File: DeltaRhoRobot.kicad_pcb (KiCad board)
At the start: 4 copper layers, 75 x 100 mm, 121 parts, among them J1 Conn_01x02_Socket, J10 Conn_01x02, J11 Conn_01x08, J12 USB_C_Receptacle_USB2.0, J13 Conn_02x09_Top_Bottom, J14 Conn_01x09, J15 Conn_02x09_Top_Bottom, J2 USB_C_Receptacle_USB2.0, J3 USB_C_Receptacle_USB2.0, J4 B4B-ZRLFSN, J5 B4B-ZRLFSN, J6 Conn_01x09, J7 Conn_02x20_Counter_Clockwise, P1 B6B-ZRLFSN, P2 B6B-ZRLFSN, P3 B6B-ZRLFSN, P4 S6B-ZRLFSN, P5 B6B-ZRLFSN, P6 B6B-ZRLFSN, Q1 MBT3904DW1, Q2 BSS138, Q3 STB55NF06T4, Q5 BSS138, SW1 CAS-120A1, SW4 SW_Push, U1 AP63205WU-7, U10 ICM-20948, U11 FT231XS, U12 ESP32-CAM, U13 MIC5365-3.3YC5, U2 AMS1117-3.3, U3 DRV8835DSSR, U4 RP2040, U5 DRV8835DSSR, U6 DRV8835DSSR, U7 W25X40CLSS, U8 ESP32-S3-WROOM-1-N8R2, Y1 ABM8G-12.000MHZ-4Y-T3

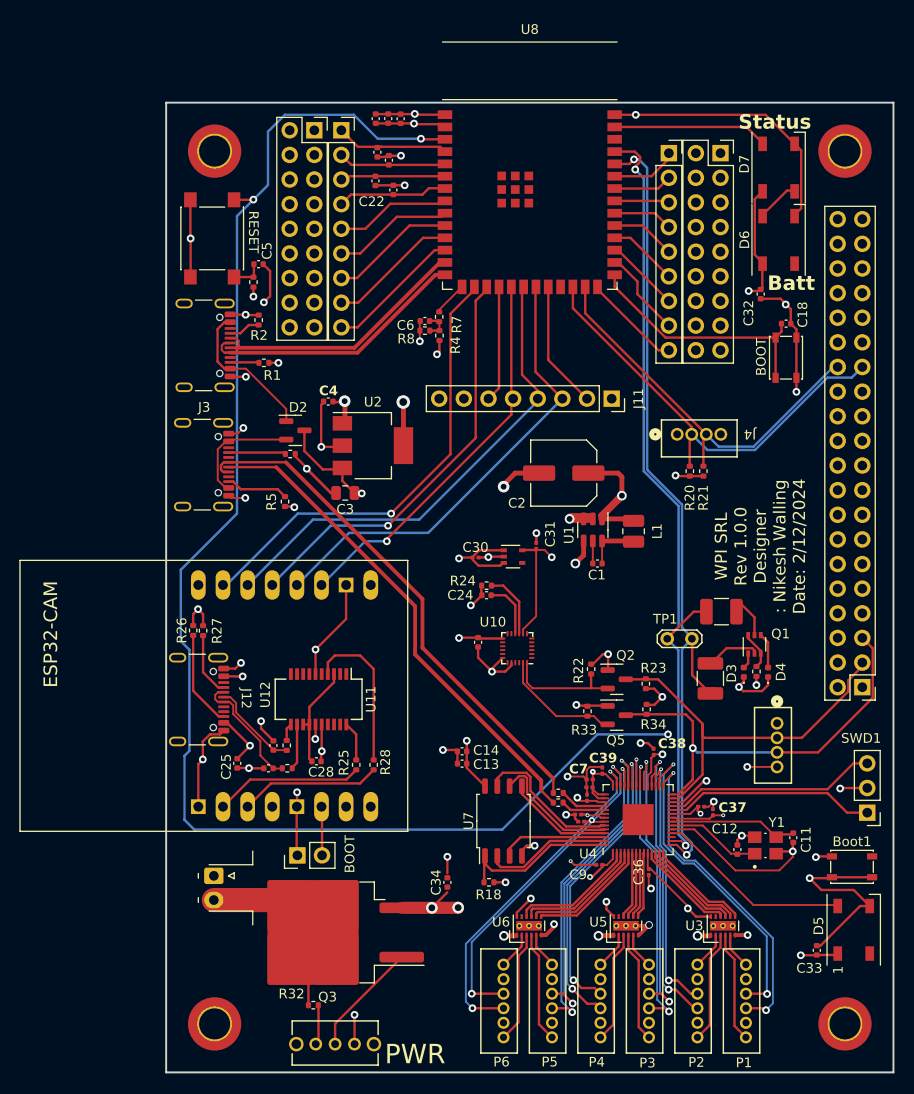
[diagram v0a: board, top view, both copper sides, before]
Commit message: Removed 201-sized parts
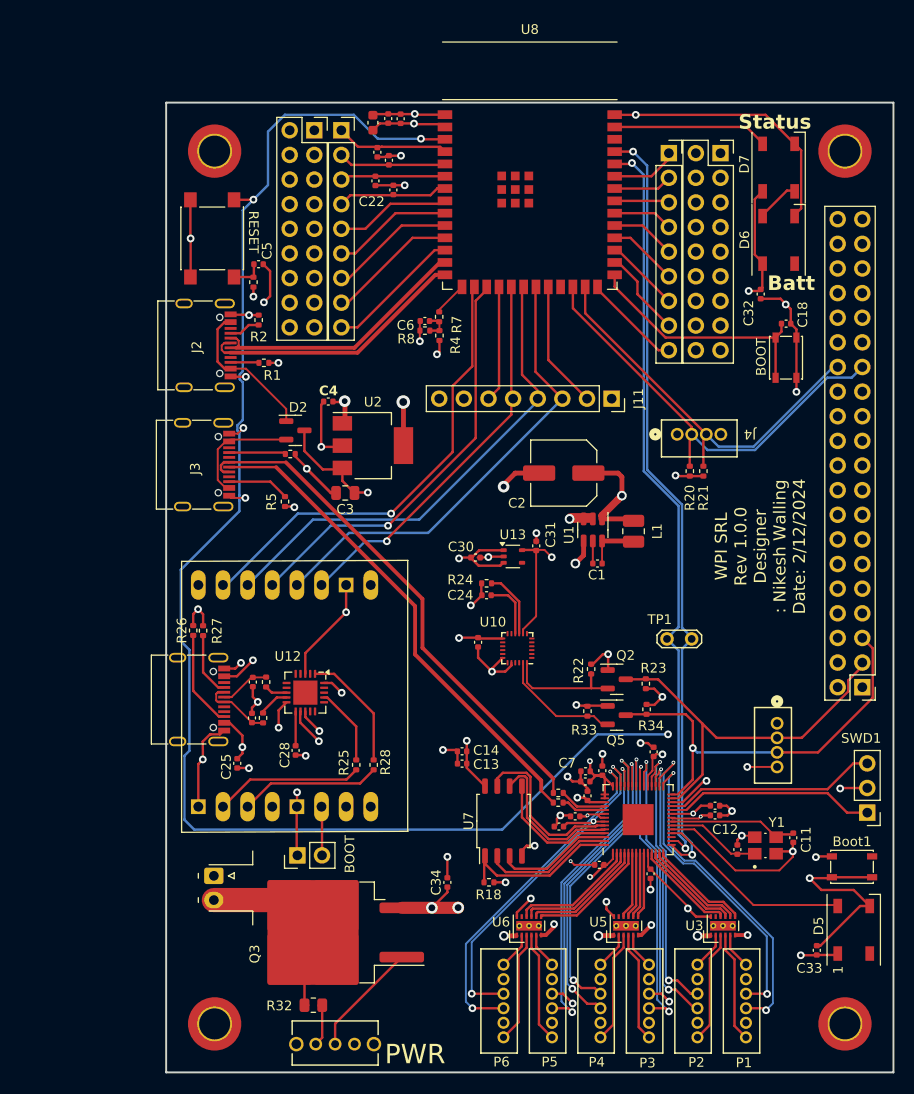
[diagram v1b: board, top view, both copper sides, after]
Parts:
- removed D3, D4: LED, LED_SMD:LED_0402_1005Metric
- removed Q1: MBT3904DW1, Package_TO_SOT_SMD:SOT-363_SC-70-6
- removed R10: 220, Resistor_SMD:R_0402_1005Metric
- removed R12, R13: 1k, Resistor_SMD:R_1210_3225Metric_Pad1.30x2.65mm_HandSolder
- removed U11: FT231XS, Package_SO:SSOP-20_3.9x8.7mm_P0.635mm
- added U9: FT231XQ, Package_DFN_QFN:QFN-20-1EP_4x4mm_P0.5mm_EP2.5x2.5mm, F.Cu at (164.4, 110.8)
- C10, C30, C31, C35, C36, C37, C38, C39, C40, C41, C42, C7, C9: footprint Capacitor_SMD:C_0201_0603Metric -> Capacitor_SMD:C_0402_1005Metric
- C11, C12: value 15p -> 15pF
- C14: value 100n -> 100nF
- C15, C18, C19, C20, C21, C22, C28: value 0.1uF -> 100nF
- C16: value 1uf -> 1uF
- C17: footprint Capacitor_SMD:C_0402_1005Metric -> Capacitor_SMD:C_0603_1608Metric
- C23, C24: value 0.1uf -> 100nF
- C34: value .1uf -> 100nF
- C5: value .1uF -> 100nf
- J12, J2, J3: footprint Connector_USB:USB_C_Receptacle_GCT_USB4105-xx-A_16P_TopMnt_Horizontal -> Connector_USB:USB_C_Receptacle_G-Switch_GT-USB-7010ASV
- R32: value 68k -> 66.5k; footprint Resistor_SMD:R_0402_1005Metric -> Resistor_SMD:R_0805_2012Metric
- R4: value 10k -> 22k
- Y1: value ABM8G-12.000MHZ-4Y-T3 -> FL1200060
- moved C26 6.87 mm to (158.9, 109.8), turned to -90 degrees
- moved R30 6.87 mm to (160.3, 109.7), turned to 90 degrees
- moved R29 5.76 mm to (160.0, 113.5), turned to 90 degrees
- moved C27 5.47 mm to (158.8, 113.5), turned to 90 degrees
- moved TP1 2.57 mm to (201.7, 105.3), turned to 0 degrees
- moved C28 2.42 mm to (163.3, 116.8), turned to -90 degrees
- moved C42 2.36 mm to (190.5, 124.7)
- moved C10 1.41 mm to (206.6, 122.5)
- moved C7 0.95 mm to (193.2, 119.0)
- moved C41 0.74 mm to (193.2, 120.0)
- moved C17 0.51 mm to (171.3, 52.1)
- moved C37 0.39 mm to (206.6, 123.5), turned to 180 degrees
- moved C40 0.36 mm to (192.2, 123.6)
- moved C36 0.25 mm to (199.9, 129.5)
- moved R24 0.24 mm to (183.0, 99.6)
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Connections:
- C28 pad 1: /ESP32-S3-WROOM-1/ESP32CAM/3.3V_Out -> Net-(U9-~{RESET})
- R29 pad 2: /ESP32-S3-WROOM-1/ESP32CAM/3.3V_Out -> Net-(U9-USBDM)
- R30 pad 1: /ESP32-S3-WROOM-1/ESP32CAM/3.3V_Out -> Net-(U9-USBDP)
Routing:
- net Earth: track 233.4 -> 222.0 mm
- net Pico_SDA1: track 86.9 -> 77.1 mm
- net /ESP32-S3-WROOM-1/ESP32CAM/V_USB: track 23.2 -> 29.1 mm
- net /ESP32-S3-WROOM-1/ESP32CAM/ESPCAM_USB_D-: track 12.7 -> 7.32 mm
- net Net-(Q1A-B1): track 4.76 -> 0.00 mm
- net /ESP32-S3-WROOM-1/ESP32CAM/ESPCAM_USB_D+: track 9.30 -> 5.18 mm
- net Net-(Q1A-C1): track 3.96 -> 0.00 mm
- net Net-(U9-TXD): track 4.08 -> 8.00 mm
- net Net-(Q1B-B2): track 3.92 -> 0.00 mm
- net Net-(D4-A): track 3.65 -> 0.00 mm
- net Net-(U9-RXD): track 16.2 -> 12.5 mm
- net Pico_SCL1: track 84.0 -> 80.4 mm
- net Net-(U9-~{RESET}): track 0.00 -> 3.56 mm
- net Net-(U9-USBDM): track 0.00 -> 3.19 mm
- net /ESP32-S3-WROOM-1/ESP32CAM/3.3V_Out: track 17.3 -> 14.5 mm, vias 0 -> 2
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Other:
- board text removed: "If UART R=1k"

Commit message: Replacing ICM-20948
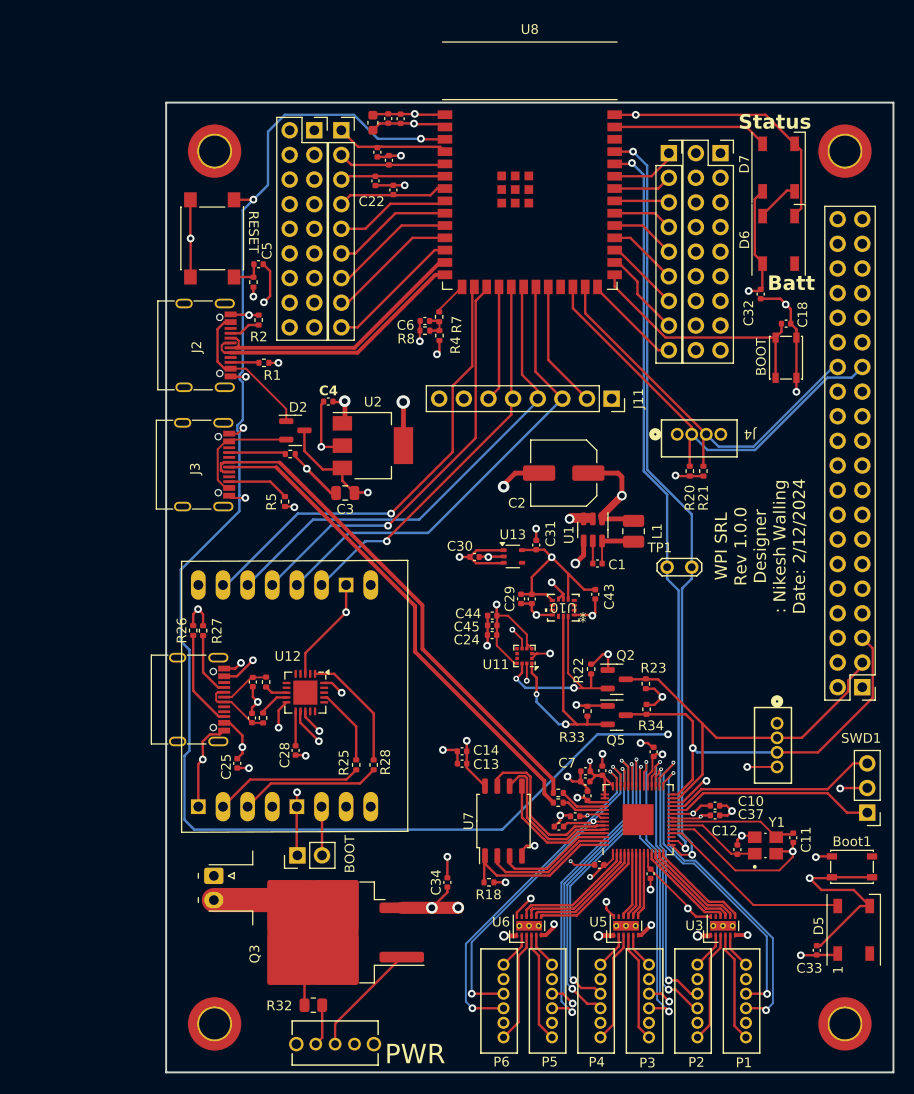
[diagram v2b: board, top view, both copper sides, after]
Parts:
- removed R24: 47, Resistor_SMD:R_0402_1005Metric
- added C29: 2.2uF, Capacitor_SMD:C_0402_1005Metric, F.Cu at (186.6, 101.2)
- added C43: 10nF, Capacitor_SMD:C_0402_1005Metric, F.Cu at (194.2, 100.7)
- added C44: 100nF, Capacitor_SMD:C_0402_1005Metric, F.Cu at (183.6, 102.9)
- added C45: 1uF, Capacitor_SMD:C_0402_1005Metric, F.Cu at (183.6, 103.9)
- added U11: LIS3MDL, Package_LGA:LGA-12_2x2mm_P0.5mm, F.Cu at (186.9, 107.1)
- U10: value ICM-20948 -> ICM-42688-P; footprint Sensor_Motion:InvenSense_QFN-24_3x3mm_P0.4mm -> ICM-42688:LGA14_2P5X3X0P91_TDK
- moved TP1 7.40 mm to (201.7, 97.9)
- moved C23 7.12 mm to (187.7, 101.2)
- moved U10 6.33 mm to (191.0, 102.1)
- moved C24 4.14 mm to (183.6, 104.9)
- moved C30 0.12 mm to (181.8, 96.8)
- moved C31 0.09 mm to (188.2, 95.6)
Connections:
- C23 pad 1: +3.3V -> +1V8
- C24 pad 1: Net-(U10-REGOUT) -> +3.3V
- U10 pad 1: unconnected-(U10-NC-Pad1) -> Earth
- U10 pad 10: Net-(U10-REGOUT) -> unconnected-(U10-RESV-Pad10)
- U10 pad 11: unconnected-(U10-FSYNC-Pad11) -> Earth
- U10 pad 12: unconnected-(U10-INT1-Pad12) -> +1V8
- U10 pad 13: +3.3V -> /Pico/IMU/SCL
- U10 pad 14: unconnected-(U10-NC-Pad14) -> /Pico/IMU/SDA
- U10 pad 5: unconnected-(U10-NC-Pad5) -> +1V8
- U10 pad 6: unconnected-(U10-NC-Pad6) -> Earth
- U10 pad 7: unconnected-(U10-AUX_CL-Pad7) -> Earth
- U10 pad 9: Net-(U10-SDO/AD0) -> unconnected-(U10-INT2/FSYNC/CLKIN-Pad9)
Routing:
- net +1V8: track 42.2 -> 59.7 mm, vias 3 -> 4
- net /Pico/IMU/SCL: track 11.9 -> 25.1 mm, vias 0 -> 2
- net /Pico/IMU/SDA: track 11.6 -> 20.6 mm, vias 0 -> 2
- net +3.3V: track 84.1 -> 92.5 mm
- net Earth: track 222.0 -> 229.9 mm, vias 50 -> 54
- net Net-(U10-SDO/AD0): track 6.89 -> 0.00 mm
- net Net-(U10-REGOUT): track 6.16 -> 0.00 mm
- net VS: track 10.7 -> 9.58 mm
- net /ESP32-S3-WROOM-1/GPIO_18: track 13.5 -> 12.8 mm
- net Pico_SDA1: track 77.1 -> 76.5 mm
- net Net-(SW1-A): track 4.03 -> 3.49 mm

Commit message: For production
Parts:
- C13: value 2.2u -> 2.2uF
- C17: value 22uf -> 22uF
- C35, C41: value 1uf -> 1uF
- C5: value 100nf -> 100nF
- R15, R16, R29, R30: value 27 -> 33
- R18: value 1k -> 1K
- R20, R21: value 5k -> 5K
- R32: value 66.5k -> 68k
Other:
- outline, holes or cut-outs redrawn
- board text added: "WPI SRL Rev 1.0.0 Designer: Nikesh Walling Date: 5/20/2024"
- board text added: "X"
- board text added: "Y"
- board text added: "Z"
- board text removed: "WPI SRL Rev 1.0.0 Designer : Nikesh Walling Date: 2/12/2024"

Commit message: JLCniceness
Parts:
- J4, J5: value B4B-ZRLFSN -> JST-XH; footprint JST-ZR-4Pin:CONN_B4B-ZRLFSN_JST -> Connector_JST:JST_XH_B4B-XH-AM_1x04_P2.50mm_Vertical
- moved R20 9.01 mm to (212.6, 85.3), turned to 180 degrees
- moved R21 8.82 mm to (212.6, 82.9), turned to 0 degrees
- moved J4 6.56 mm to (204.7, 90.5), turned to 90 degrees
- moved J5 3.93 mm to (210.3, 116.8)
- moved R2 0.96 mm to (160.3, 73.0)
- moved C15 0.54 mm to (174.1, 52.2)
- moved C16 0.54 mm to (172.8, 52.2)
- moved C17 0.54 mm to (171.2, 52.6)
- moved C18 0.52 mm to (213.4, 72.8)
- moved SW4 0.52 mm to (213.4, 76.3)
- moved R30 0.32 mm to (160.0, 109.8)
- moved C26 0.09 mm to (158.8, 109.8)
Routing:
- net PICO_SCL: track 43.2 -> 37.1 mm
- net +5V: track 136.8 -> 132.6 mm
- net /Pico/M5_Enc_B: track 32.4 -> 35.4 mm
- net Earth: track 229.8 -> 232.5 mm, vias 54 -> 50
- net /V_USB_2: track 11.2 -> 13.9 mm, vias 0 -> 2
- net /ESP32-S3-WROOM-1/SCL: track 40.4 -> 38.4 mm
- net +3.3V: track 92.5 -> 90.5 mm, vias 17 -> 18
- net /Pico/M4_Enc_A: track 31.9 -> 33.7 mm
- net /Pico/M5_Enc_A: track 33.9 -> 35.5 mm
- net /Pico/M3_Enc_A: track 30.7 -> 32.2 mm
- net /V_USB_1: track 15.3 -> 16.4 mm, vias 0 -> 2
- net /Pico/M4_Enc_B: track 32.3 -> 33.4 mm
- net PICO_SDA: track 40.1 -> 39.1 mm
- net /Pico/M6_Enc_A: track 35.6 -> 34.7 mm
- net /Pico/M3_Enc_B: track 30.7 -> 31.5 mm
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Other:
- board text added: "WPI SRL Rev 1.0.1 Designer: Nikesh Walling Date: 5/20/2024"
- board text removed: "WPI SRL Rev 1.0.0 Designer: Nikesh Walling Date: 5/20/2024"

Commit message: JLC fixes
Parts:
- J4, J5: footprint Connector_JST:JST_XH_B4B-XH-AM_1x04_P2.50mm_Vertical -> Connector_JST:JST_XH_B4B-XH-A_1x04_P2.50mm_Vertical
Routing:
- net /Pico/M5_Enc_B: track 35.4 -> 39.2 mm
- net /ESP_PU: track 166.1 -> 168.8 mm
- net +1V8: track 59.6 -> 62.2 mm, vias 4 -> 5
- net /Pico/M6_Enc_A: track 34.7 -> 37.2 mm
- net /Pico/M3_Enc_B: track 31.5 -> 33.2 mm
- net /Pico/M4_Enc_B: track 33.4 -> 35.0 mm
- net +3.3V: track 90.5 -> 89.0 mm
- net /Pico/M2_Enc_A: track 27.7 -> 29.0 mm
- net /ESP32-S3-WROOM-1/ESP_MOSI: track 40.2 -> 41.2 mm
- net /ESP32-S3-WROOM-1/Handshake: track 46.4 -> 47.3 mm
- net /ESP32-S3-WROOM-1/ESP_CS1: track 43.0 -> 43.9 mm
- net /Pico/M5_Enc_A: track 35.5 -> 34.5 mm
- net /Pico/M6_Enc_B: track 35.9 -> 36.8 mm
- net /V_USB_2: track 13.9 -> 14.6 mm
- net Earth: track 232.5 -> 233.2 mm
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
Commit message: Rev 2 PCB
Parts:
- removed C34: 100nF, Capacitor_SMD:C_0402_1005Metric
- removed D2: PMEG2005CT, Package_TO_SOT_SMD:SOT-23
- removed Q3: STB55NF06T4, Package_TO_SOT_SMD:TO-263-2
- removed R32: 68k, Resistor_SMD:R_0805_2012Metric
- removed U1: AP63205WU-7, Package_TO_SOT_SMD:TSOT-23-6
- added C46: 100nF, Capacitor_SMD:C_0402_1005Metric, F.Cu at (190.3, 93.9)
- added C47: 22uF, Capacitor_SMD:C_0805_2012Metric, F.Cu at (191.1, 85.6)
- added C48: 10uF, Capacitor_SMD:C_0402_1005Metric, F.Cu at (189.2, 93.9)
- added C49: 100nF, Capacitor_SMD:C_0402_1005Metric, F.Cu at (189.2, 86.7)
- added C50: 22uF, Capacitor_SMD:C_0805_2012Metric, F.Cu at (164.3, 133.8)
- added C51: 22uF, Capacitor_SMD:C_0805_2012Metric, F.Cu at (197.6, 85.6)
- added C52: 22uF, Capacitor_SMD:C_0805_2012Metric, F.Cu at (193.3, 85.6)
- added C53: 22uF, Capacitor_SMD:C_0805_2012Metric, F.Cu at (195.5, 85.6)
- added C54: 22uF, Capacitor_SMD:C_0805_2012Metric, F.Cu at (161.0, 133.8)
- added D1: PMEG2005CT, Package_TO_SOT_SMD:SOT-23, F.Cu at (163.3, 83.8)
- added MOSFET1: AONR21321, AONR:DFN8_3x3_EP_AOS, F.Cu at (168.4, 137.5)
- added R10: 30K, Resistor_SMD:R_0402_1005Metric, F.Cu at (197.4, 92.0)
- added R11: R_US, Resistor_SMD:R_0402_1005Metric, F.Cu at (209.5, 124.2)
- added R12: 27, Resistor_SMD:R_0402_1005Metric, F.Cu at (167.4, 142.3)
- added R13: 100K, Resistor_SMD:R_0402_1005Metric, F.Cu at (193.9, 96.1)
- added R17: DNF, Resistor_SMD:R_0603_1608Metric_Pad0.98x0.95mm_HandSolder, F.Cu at (179.7, 121.5)
- added R19: 33.2K, Resistor_SMD:R_0402_1005Metric, F.Cu at (193.9, 97.3)
- added R3: 220K, Resistor_SMD:R_0402_1005Metric, F.Cu at (196.9, 90.2)
- added R9: 1K, Resistor_SMD:R_0402_1005Metric, F.Cu at (163.0, 142.3)
- added TP2: TestPoint, TestPoint:TestPoint_Pad_D1.5mm, F.Cu at (179.5, 127.8)
- added U14: W25Q16JVS, Package_SO:SOIC-8_5.23x5.23mm_P1.27mm, F.Cu at (184.8, 124.0)
- C1: value 100nF -> 10uF
- C2: value 22uF -> 33pF; footprint Capacitor_SMD:C_Elec_6.3x5.8 -> Capacitor_SMD:C_0402_1005Metric
- C3: footprint Capacitor_SMD:C_0805_2012Metric -> Capacitor_SMD:C_0402_1005Metric
- L1: value 4.7uH -> 2.2uH
- P4: value S6B-ZRLFSN -> B6B-ZRLFSN
- R16: value 33 -> 27
- U7: value W25X40CLSS -> TPS566242DRLR; footprint Package_SO:SOIC-8_5.275x5.275mm_P1.27mm -> Package_TO_SOT_SMD:SOT-23-6
- U8: footprint Espressif:ESP32-S3-WROOM-1 -> PCM_Espressif:ESP32-S3-WROOM-1
- Y1: value FL1200060 -> ABM8-272-T3; footprint ABM8G:XTAL_ABM8G-12.000MHZ-4Y-T3 -> Oscillator:Oscillator_SMD_Abracon_ASE-4Pin_3.2x2.5mm
- moved U7 33.0 mm to (194.0, 92.4), turned to 0 degrees
- moved R20 22.8 mm to (192.9, 73.9), turned to 90 degrees
- moved R21 19.3 mm to (195.4, 74.1), turned to -90 degrees
- moved L1 9.64 mm to (189.3, 90.5)
- moved C2 7.38 mm to (198.1, 90.2), turned to -90 degrees
- moved C1 7.25 mm to (188.2, 93.9), turned to -90 degrees
- moved J4 4.88 mm to (209.6, 90.4)
- moved C4 3.97 mm to (170.3, 79.1), turned to 180 degrees
- moved C31 3.32 mm to (188.7, 98.9), turned to -90 degrees
- moved R26 2.97 mm to (155.7, 103.9), turned to 0 degrees
- moved J1 2.00 mm to (154.3, 131.7)
- moved R27 1.95 mm to (155.7, 104.9), turned to 0 degrees
- moved C30 1.92 mm to (181.3, 98.7), turned to 90 degrees
- moved U13 1.81 mm to (184.6, 98.2)
- moved C42 1.24 mm to (189.6, 123.8), turned to 90 degrees
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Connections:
- C1 pad 1: Net-(U1-SW) -> VCC
- C1 pad 2: Net-(U1-BST) -> Earth
- C11 pad 1: /Pico/XOUT -> Net-(C11-Pad1)
- C2 pad 2: Earth -> Net-(U7-FB)
- C3 pad 1: VCC -> +5V
- J1 pad 2: VS -> VIN
- J11 pad 8: VCC -> +5V
- L1 pad 1: Net-(U1-BST) -> Net-(U7-SW)
- U2 pad 3: VCC -> +5V
- U7 pad 1: /Pico/QSPI_SDSS -> Earth
- U7 pad 2: /Pico/QSPI_SD1 -> Net-(U7-SW)
- U7 pad 3: /Pico/QSPI_SD2 -> VCC
- U7 pad 5: /Pico/QSPI_SD0 -> Net-(U7-EN)
- U7 pad 6: /Pico/QSPI_SCK -> Net-(U7-FB)
- Y1 pad 3: /Pico/XOUT -> Net-(C11-Pad1)
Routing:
- net +5V: track 132.6 -> 199.7 mm, vias 3 -> 5
- net VIN: track 0.00 -> 26.6 mm
- net /ESP_PU: track 168.8 -> 154.5 mm
- net VS: track 9.58 -> 0.00 mm
- net Earth: track 233.2 -> 242.7 mm, vias 50 -> 61
- net Net-(Boot1-Pad1): track 36.0 -> 45.4 mm
- net VCC: track 143.8 -> 136.4 mm
- net Net-(SW1-B): track 11.3 -> 4.12 mm
- net /Pico/XOUT: track 13.0 -> 6.83 mm
- net Net-(U1-BST): track 5.49 -> 0.00 mm
- net Net-(U7-EN): track 0.00 -> 5.24 mm
- net Net-(C11-Pad1): track 0.00 -> 5.05 mm
- net Net-(U7-FB): track 0.00 -> 4.52 mm
- net /Pico/QSPI_SDSS: track 17.0 -> 20.9 mm
- net +3.3V: track 89.0 -> 92.9 mm, vias 18 -> 17
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- added copper zone on F.Cu, net Earth
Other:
- board text added: "WPI SRL Rev 2.0.0 Designer: Nikesh Walling Date: 6/10/2024"
- board text removed: "WPI SRL Rev 1.0.1 Designer: Nikesh Walling Date: 5/20/2024"

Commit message: Cleaning up
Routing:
- net VCC: track 136.4 -> 132.9 mm
- net /Pico/M5_Enc_B: track 36.8 -> 34.1 mm
- net /Pico/M3_Enc_A: track 34.5 -> 32.0 mm
- net /Pico/M5_Enc_A: track 34.5 -> 33.3 mm
- net /Pico/M3_Enc_B: track 33.4 -> 32.2 mm
- net /Pico/M4_Enc_A: track 34.4 -> 35.5 mm
- net /Pico/M6_Enc_B: track 36.8 -> 35.8 mm
- net /Pico/M6_Enc_A: track 37.2 -> 36.3 mm
- net /Pico/QSPI_SDSS: track 20.9 -> 20.3 mm
- net /Pico/M4_Enc_B: track 34.6 -> 35.1 mm
- net Pico_SCL1: track 80.6 -> 80.1 mm
- net Earth: track 242.7 -> 242.9 mm, vias 61 -> 57
- added copper zone on F.Cu, net VCC
